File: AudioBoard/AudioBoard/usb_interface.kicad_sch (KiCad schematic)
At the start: 3 parts, among them J11 USB_C_Receptacle_USB2.0, U23 USBLC6-2P6

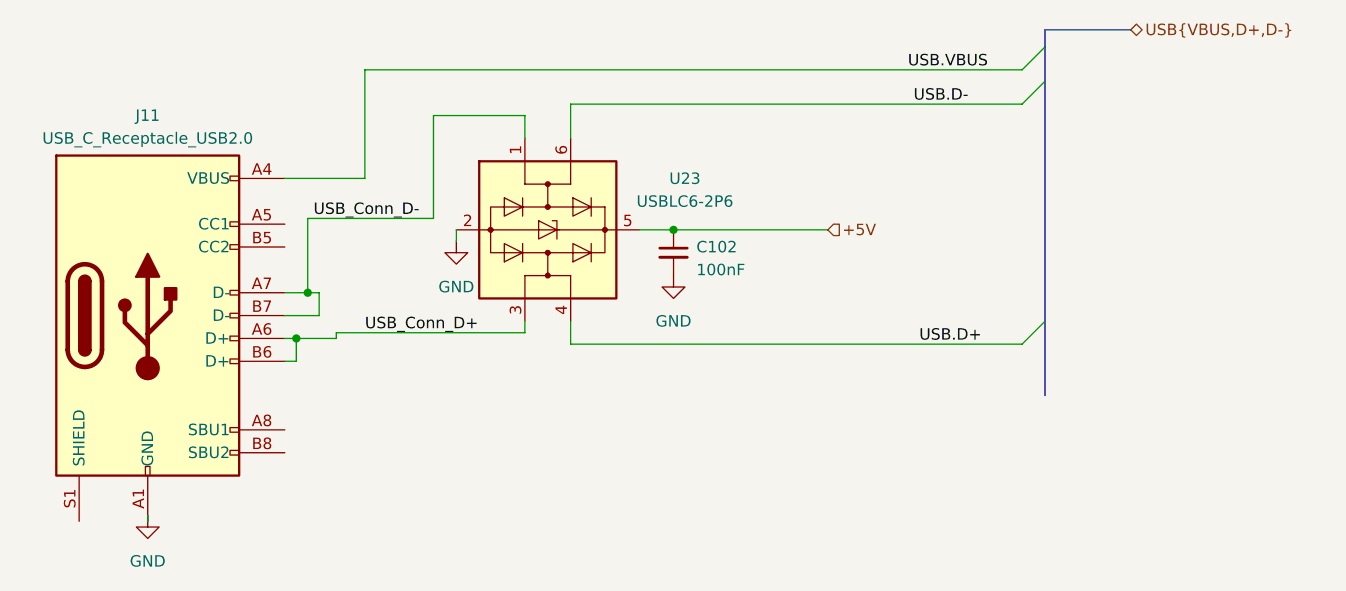
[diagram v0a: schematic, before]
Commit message: modified clamping diodes on inputs, added exp pedal input filter, added ideas to instrument input filter redesign
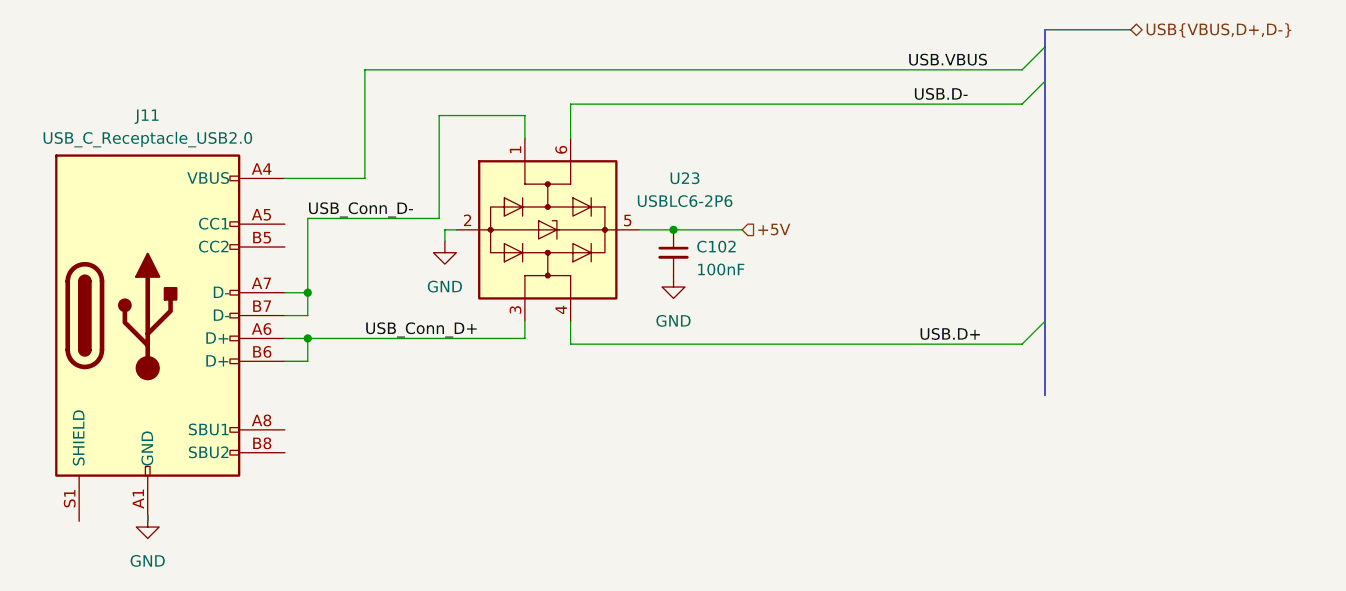
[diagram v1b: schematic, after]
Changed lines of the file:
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@@
 	(paper "A4")
 	(junction
-		(at 110.49 73.66)
+		(at 111.76 73.66)
+		(diameter 0)
+		(color 0 0 0 0)
+	)
+	(junction
+		(at 111.76 68.58)
 		(diameter 0)
 		(color 0 0 0 0)
@@
 		(color 0 0 0 0)
 	)
-	(junction
-		(at 111.76 68.58)
-		(diameter 0)
-		(color 0 0 0 0)
-	)
 	(bus_entry
 		(at 193.675 41.275)
@@
 	(wire
 		(pts
-			(xy 109.22 71.12) (xy 113.03 71.12)
-		)
-		(stroke
-			(width 0)
-			(type default)
-		)
-	)
-	(wire
-		(pts
-			(xy 111.76 68.58) (xy 113.03 68.58)
-		)
-		(stroke
-			(width 0)
-			(type default)
-		)
-	)
-	(wire
-		(pts
-			(xy 135.89 73.025) (xy 135.89 71.755)
+			(xy 109.22 71.12) (xy 111.76 71.12)
+		)
+		(stroke
+			(width 0)
+			(type default)
+		)
+	)
+	(wire
+		(pts
+			(xy 135.89 73.66) (xy 135.89 71.755)
 		)
 		(stroke
@@
 	(wire
 		(pts
-			(xy 169.545 61.595) (xy 152.4 61.595)
+			(xy 127 61.595) (xy 128.27 61.595)
+		)
+		(stroke
+			(width 0)
+			(type default)
+		)
+	)
+	(wire
+		(pts
+			(xy 160.02 61.595) (xy 152.4 61.595)
 		)
 		(stroke
@@
 	(wire
 		(pts
-			(xy 111.76 60.325) (xy 125.73 60.325)
+			(xy 111.76 60.325) (xy 126.365 60.325)
 		)
 		(stroke
@@
 	(wire
 		(pts
-			(xy 113.03 68.58) (xy 113.03 71.12)
-		)
-		(stroke
-			(width 0)
-			(type default)
-		)
-	)
-	(wire
-		(pts
-			(xy 125.73 48.895) (xy 135.89 48.895)
+			(xy 111.76 68.58) (xy 111.76 71.12)
+		)
+		(stroke
+			(width 0)
+			(type default)
+		)
+	)
+	(wire
+		(pts
+			(xy 126.365 48.895) (xy 135.89 48.895)
 		)
 		(stroke
@@
 	(wire
 		(pts
-			(xy 110.49 73.66) (xy 114.935 73.66)
-		)
-		(stroke
-			(width 0)
-			(type default)
-		)
-	)
-	(wire
-		(pts
-			(xy 109.22 73.66) (xy 110.49 73.66)
+			(xy 109.22 73.66) (xy 111.76 73.66)
 		)
 		(stroke
@@
 	(wire
 		(pts
-			(xy 128.27 62.865) (xy 128.27 61.595)
+			(xy 111.76 73.66) (xy 135.89 73.66)
+		)
+		(stroke
+			(width 0)
+			(type default)
+		)
+	)
+	(wire
+		(pts
+			(xy 127 62.865) (xy 127 61.595)
 		)
 		(stroke
@@
 	(wire
 		(pts
-			(xy 109.22 76.2) (xy 110.49 76.2)
+			(xy 109.22 76.2) (xy 111.76 76.2)
 		)
 		(stroke
@@
 	(wire
 		(pts
-			(xy 114.935 73.66) (xy 114.935 73.025)
-		)
-		(stroke
-			(width 0)
-			(type default)
-		)
-	)
-	(wire
-		(pts
 			(xy 111.76 60.325) (xy 111.76 68.58)
 		)
@@
 	(wire
 		(pts
-			(xy 110.49 73.66) (xy 110.49 76.2)
-		)
-		(stroke
-			(width 0)
-			(type default)
-		)
-	)
-	(wire
-		(pts
-			(xy 114.935 73.025) (xy 135.89 73.025)
+			(xy 111.76 73.66) (xy 111.76 76.2)
 		)
 		(stroke
@@
 	(wire
 		(pts
-			(xy 125.73 48.895) (xy 125.73 60.325)
+			(xy 126.365 48.895) (xy 126.365 60.325)
 		)
 		(stroke
@@
 	)
 	(label "USB_Conn_D-"
-		(at 112.395 60.325 0)
+		(at 111.76 60.325 0)
 		(effects
 			(font
@@
 	)
 	(label "USB_Conn_D+"
-		(at 118.11 73.025 0)
+		(at 118.11 73.66 0)
 		(effects
 			(font
@@
 	(hierarchical_label "+5V"
 		(shape input)
-		(at 169.545 61.595 0)
+		(at 160.02 61.595 0)
 		(effects
 			(font
@@
 	(symbol
 		(lib_id "power:GND")
-		(at 128.27 62.865 0)
+		(at 127 62.865 0)
 		(unit 1)
 		(body_style 1)
@@
 		(fields_autoplaced yes)
 		(property "Reference" "#PWR0190"
-			(at 128.27 69.215 0)
+			(at 127 69.215 0)
 			(hide yes)
 			(show_name no)
@@
 		)
 		(property "Value" "GND"
-			(at 128.27 67.945 0)
+			(at 127 67.945 0)
 			(show_name no)
 			(do_not_autoplace no)
@@
 		)
 		(property "Footprint" ""
-			(at 128.27 62.865 0)
+			(at 127 62.865 0)
 			(hide yes)
 			(show_name no)
@@
 		)
 		(property "Datasheet" ""
-			(at 128.27 62.865 0)
+			(at 127 62.865 0)
 			(hide yes)
 			(show_name no)
@@
 		)
 		(property "Description" ""
-			(at 128.27 62.865 0)
-			(show_name no)
-			(do_not_autoplace no)
+			(at 127 62.865 0)
+			(show_name no)
+			(do_not_autoplace no)
